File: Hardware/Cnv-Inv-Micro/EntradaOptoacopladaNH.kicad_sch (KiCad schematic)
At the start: 3 parts, among them U19 PC817

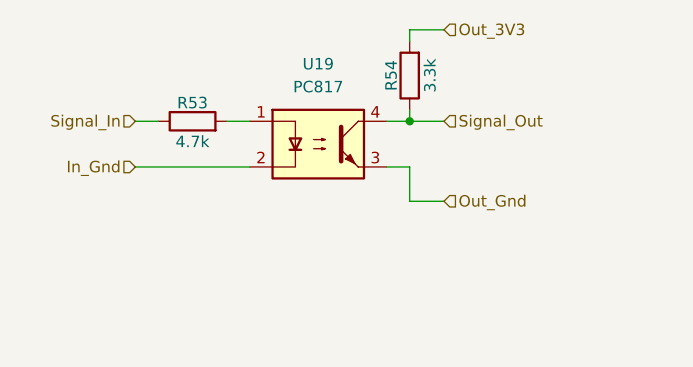
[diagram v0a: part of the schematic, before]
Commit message: Avances en PCB conversor y inversor - Simulaciones de modulacion
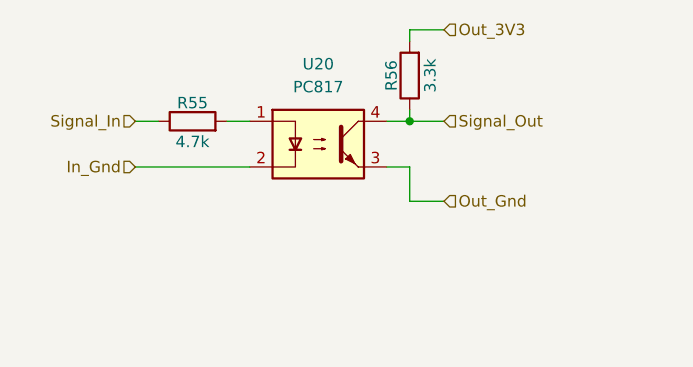
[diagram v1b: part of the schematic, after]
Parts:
- renumbered R53 to R55, R54 to R56, U19 to U20
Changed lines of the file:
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@@
 		(on_board yes)
 		(dnp no)
-		(property "Reference" "R54"
+		(property "Reference" "R56"
 			(at 112.268 76.2 90)
 			(effects
@@
 			(project "VFD_V1"
 				(path "/e60c11d9-ab9e-4760-a4a7-008fcec65a72/fc30a5fb-ff38-4397-8c78-21712589d910/15d84fde-48a5-471f-8aa3-e7a3fbba29f1"
-					(reference "R54")
+					(reference "R56")
 					(unit 1)
 				)
@@
 		(on_board yes)
 		(dnp no)
-		(property "Reference" "R53"
+		(property "Reference" "R55"
 			(at 90.17 79.248 90)
 			(effects
@@
 			(project "VFD_V1"
 				(path "/e60c11d9-ab9e-4760-a4a7-008fcec65a72/fc30a5fb-ff38-4397-8c78-21712589d910/15d84fde-48a5-471f-8aa3-e7a3fbba29f1"
-					(reference "R53")
+					(reference "R55")
 					(unit 1)
 				)
@@
 		(dnp no)
 		(fields_autoplaced yes)
-		(property "Reference" "U19"
+		(property "Reference" "U20"
 			(at 104.14 74.93 0)
 			(effects
@@
 			(project "VFD_V1"
 				(path "/e60c11d9-ab9e-4760-a4a7-008fcec65a72/fc30a5fb-ff38-4397-8c78-21712589d910/15d84fde-48a5-471f-8aa3-e7a3fbba29f1"
-					(reference "U19")
+					(reference "U20")
 					(unit 1)
 				)
